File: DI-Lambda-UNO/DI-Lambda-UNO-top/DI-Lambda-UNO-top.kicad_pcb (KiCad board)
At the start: 2 copper layers, 38.2 x 125 mm, 12 parts, among them J1 CONN_02X04, J10 CONN_02X04, J11 CONN_02X04, J12 CONN_02X04, J2 CONN_02X04, J3 CONN_02X04, J4 CONN_02X04, J5 CONN_02X04, J6 CONN_02X04, J7 CONN_02X04, J8 CONN_02X04, J9 CONN_02X04

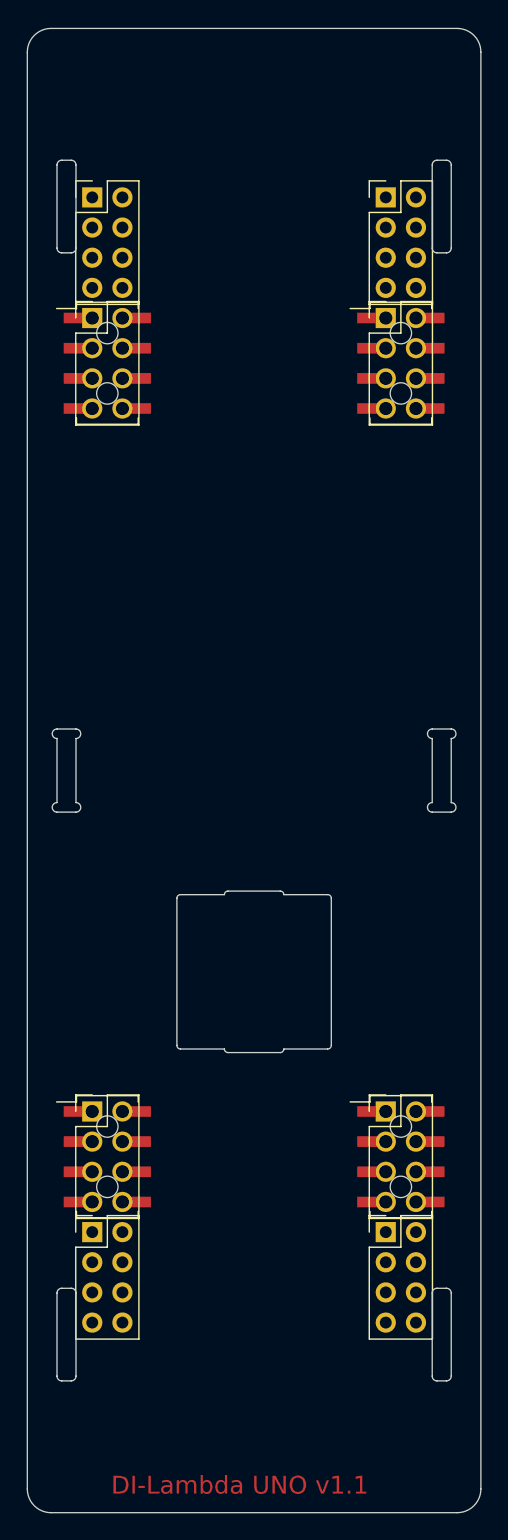
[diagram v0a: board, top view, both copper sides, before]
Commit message: Rework the top plate - STM+THT connectors and new dimensions
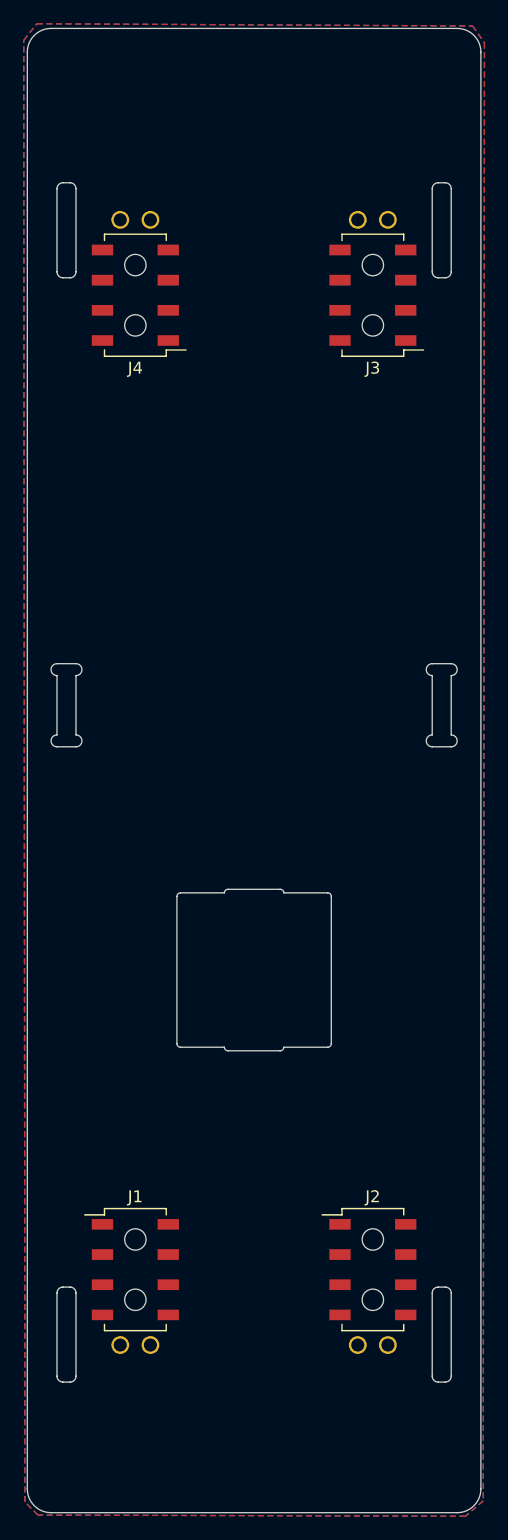
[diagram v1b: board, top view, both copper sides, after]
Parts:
- removed J10, J11, J12, J9: CONN_02X04, Female_socket_pitch254_smt_through-board:Pin_Header_Straight_2x04_Pitch2.54mm_SMD
- removed J5, J6, J7, J8: CONN_02X04, Female_sockets_254_tht:Pin_Header_Straight_2x04_Pitch2.54mm
- J1, J2, J3, J4: footprint Female_sockets_254_tht:Pin_Header_Straight_2x04_Pitch2.54mm -> Female_socket_pitch254_smt_through-board:Pin_Header_Straight_2x04_Pitch2.54mm_SMD_2THT
- moved J1 82.9 mm to (139.2, 123.3)
- moved J3 78.9 mm to (159.2, 41.2), turned to 180 degrees
- moved J2 13.4 mm to (159.2, 123.3)
- moved J4 4.11 mm to (139.2, 41.2), turned to 180 degrees
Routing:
- added copper zone on B.Cu, net (none)
- added copper zone on F.Cu, net (none)
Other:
- outline, holes or cut-outs redrawn

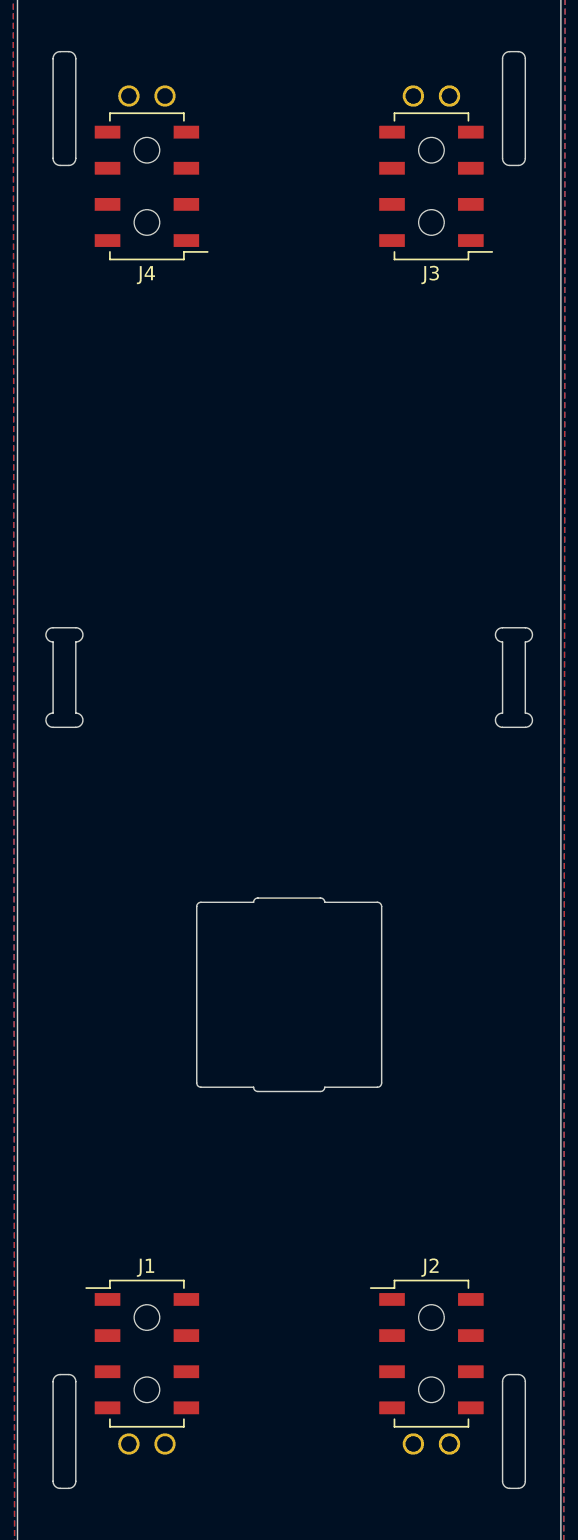
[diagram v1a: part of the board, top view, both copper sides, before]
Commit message: Update schematics to version 1.3
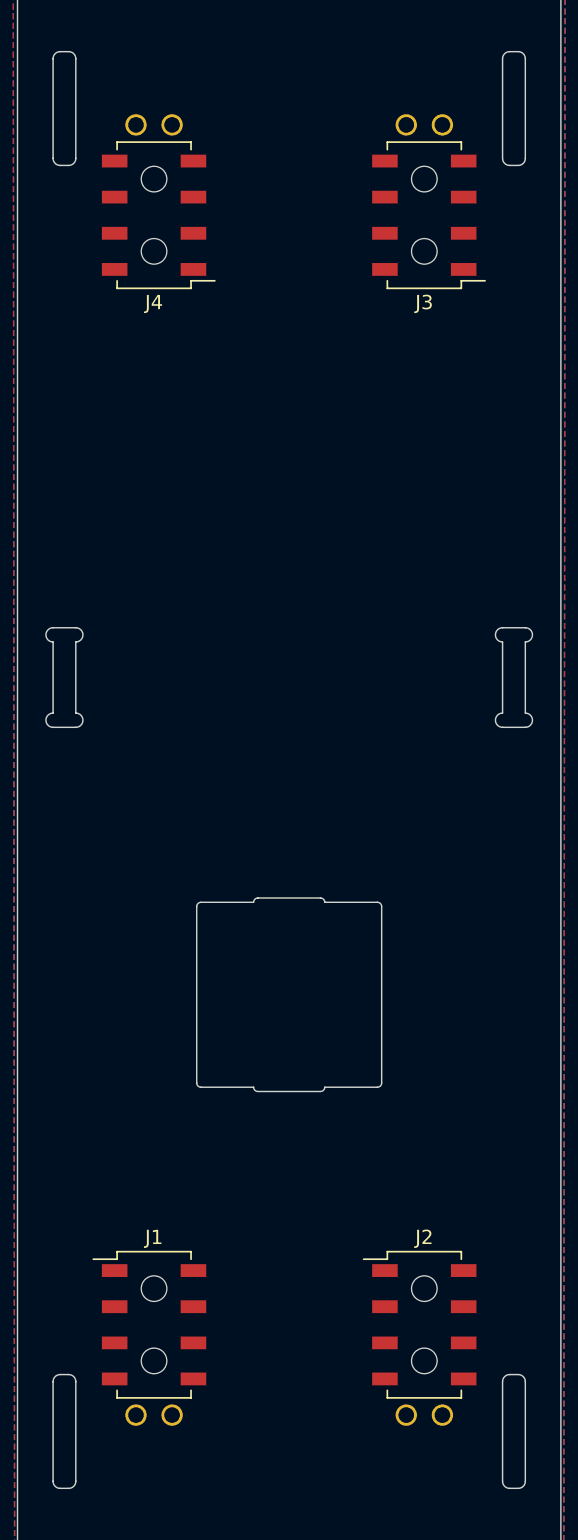
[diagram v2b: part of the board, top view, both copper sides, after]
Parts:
- moved J1 2.09 mm to (139.7, 121.3)
- moved J2 2.09 mm to (158.7, 121.3)
- moved J3 2.09 mm to (158.7, 43.3)
- moved J4 2.09 mm to (139.7, 43.3)
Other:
- board text added: "DI-Lambda UNO v1.3"
- board text removed: "DI-Lambda UNO v1.1"
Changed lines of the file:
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@@
   (general
     (thickness 1.6)
-    (drawings 90)
+    (drawings 98)
     (tracks 0)
     (zones 0)
@@
     (aux_axis_origin 0 0)
     (grid_origin 130.084 143.764)
-    (visible_elements FFFFFF7F)
+    (visible_elements FFFFEF7F)
     (pcbplotparams
       (layerselection 0x000f0_ffffffff)
@@
   )
   (module Female_socket_pitch254_smt_through-board:Pin_Header_Straight_2x04_Pitch2.54mm_SMD_2THT (layer F.Cu)
-    (at 139.184 41.234 180)
+    (at 139.684 43.264 180)
     (descr "surface-mounted straight pin header, 2x04, 2.54mm pitch, double rows")
     (tags "Surface mounted pin header SMD 2x04 2.54mm double row wirth 2 THT holes")
@@
   )
   (module Female_socket_pitch254_smt_through-board:Pin_Header_Straight_2x04_Pitch2.54mm_SMD_2THT (layer F.Cu)
-    (at 159.184 41.234 180)
+    (at 158.684 43.264 180)
     (descr "surface-mounted straight pin header, 2x04, 2.54mm pitch, double rows")
     (tags "Surface mounted pin header SMD 2x04 2.54mm double row wirth 2 THT holes")
@@
   )
   (module Female_socket_pitch254_smt_through-board:Pin_Header_Straight_2x04_Pitch2.54mm_SMD_2THT (layer F.Cu)
-    (at 159.184 123.294)
+    (at 158.684 121.264)
     (descr "surface-mounted straight pin header, 2x04, 2.54mm pitch, double rows")
     (tags "Surface mounted pin header SMD 2x04 2.54mm double row wirth 2 THT holes")
@@
   )
   (module Female_socket_pitch254_smt_through-board:Pin_Header_Straight_2x04_Pitch2.54mm_SMD_2THT (layer F.Cu)
-    (at 139.184 123.294)
+    (at 139.684 121.264)
     (descr "surface-mounted straight pin header, 2x04, 2.54mm pitch, double rows")
     (tags "Surface mounted pin header SMD 2x04 2.54mm double row wirth 2 THT holes")
@@
     (pad "" np_thru_hole circle (at 0 2.54) (size 1.8 1.8) (drill 1.8) (layers *.Cu *.Mask))
   )
+  (gr_text "DI-Lambda UNO v1.3" (at 149.184 23.164) (layer F.Mask)
+    (effects (font (size 1.5 1.5) (thickness 0.3)))
+  )
+  (gr_line (start 139.684 32.264) (end 139.684 136.864) (layer Eco1.User) (width 0.2))
+  (gr_line (start 158.684 121.264) (end 135.484 121.264) (layer Eco1.User) (width 0.2))
+  (gr_line (start 158.684 43.264) (end 135.384 43.264) (layer Eco1.User) (width 0.2))
+  (dimension 78 (width 0.3) (layer Eco1.User)
+    (gr_text "78.000 mm" (at 181.536674 82.264 90) (layer Eco1.User)
+      (effects (font (size 1.5 1.5) (thickness 0.3)))
+    )
+    (feature1 (pts (xy 158.684 43.264) (xy 182.886674 43.264)))
+    (feature2 (pts (xy 158.684 121.264) (xy 182.886674 121.264)))
+    (crossbar (pts (xy 180.186674 121.264) (xy 180.186674 43.264)))
+    (arrow1a (pts (xy 180.186674 43.264) (xy 180.773095 44.390504)))
+    (arrow1b (pts (xy 180.186674 43.264) (xy 179.600253 44.390504)))
+    (arrow2a (pts (xy 180.186674 121.264) (xy 180.773095 120.137496)))
+    (arrow2b (pts (xy 180.186674 121.264) (xy 179.600253 120.137496)))
+  )
+  (dimension 22.5 (width 0.3) (layer Eco1.User)
+    (gr_text "22.500 mm" (at 175.034 132.514 90) (layer Eco1.User)
+      (effects (font (size 1.5 1.5) (thickness 0.3)))
+    )
+    (feature1 (pts (xy 158.684 121.264) (xy 176.384 121.264)))
+    (feature2 (pts (xy 158.684 143.764) (xy 176.384 143.764)))
+    (crossbar (pts (xy 173.684 143.764) (xy 173.684 121.264)))
+    (arrow1a (pts (xy 173.684 121.264) (xy 174.270421 122.390504)))
+    (arrow1b (pts (xy 173.684 121.264) (xy 173.097579 122.390504)))
+    (arrow2a (pts (xy 173.684 143.764) (xy 174.270421 142.637496)))
+    (arrow2b (pts (xy 173.684 143.764) (xy 173.097579 142.637496)))
+  )
+  (dimension 5.5 (width 0.3) (layer Eco1.User)
+    (gr_text "5.500 mm" (at 161.423127 28.360696) (layer Eco1.User)
+      (effects (font (size 1.5 1.5) (thickness 0.3)))
+    )
+    (feature1 (pts (xy 164.173127 32.310696) (xy 164.173127 27.010696)))
+    (feature2 (pts (xy 158.673127 32.310696) (xy 158.673127 27.010696)))
+    (crossbar (pts (xy 158.673127 29.710696) (xy 164.173127 29.710696)))
+    (arrow1a (pts (xy 164.173127 29.710696) (xy 163.046623 30.297117)))
+    (arrow1b (pts (xy 164.173127 29.710696) (xy 163.046623 29.124275)))
+    (arrow2a (pts (xy 158.673127 29.710696) (xy 159.799631 30.297117)))
+    (arrow2b (pts (xy 158.673127 29.710696) (xy 159.799631 29.124275)))
+  )
+  (gr_line (start 158.684 31.964) (end 158.684 136.564) (layer Eco1.User) (width 0.2))
+  (dimension 5.5 (width 0.3) (layer Eco1.User)
+    (gr_text "5.500 mm" (at 136.934 28.314) (layer Eco1.User)
+      (effects (font (size 1.5 1.5) (thickness 0.3)))
+    )
+    (feature1 (pts (xy 139.684 32.264) (xy 139.684 26.964)))
+    (feature2 (pts (xy 134.184 32.264) (xy 134.184 26.964)))
+    (crossbar (pts (xy 134.184 29.664) (xy 139.684 29.664)))
+    (arrow1a (pts (xy 139.684 29.664) (xy 138.557496 30.250421)))
+    (arrow1b (pts (xy 139.684 29.664) (xy 138.557496 29.077579)))
+    (arrow2a (pts (xy 134.184 29.664) (xy 135.310504 30.250421)))
+    (arrow2b (pts (xy 134.184 29.664) (xy 135.310504 29.077579)))
+  )
   (dimension 20.7 (width 0.3) (layer Eco1.User)
-    (gr_text "20.700 mm" (at 138.834 114.914 90) (layer Eco1.User)
-      (effects (font (size 1.5 1.5) (thickness 0.3)))
-    )
-    (feature1 (pts (xy 142.784 104.564) (xy 137.484 104.564)))
-    (feature2 (pts (xy 142.784 125.264) (xy 137.484 125.264)))
-    (crossbar (pts (xy 140.184 125.264) (xy 140.184 104.564)))
-    (arrow1a (pts (xy 140.184 104.564) (xy 140.770421 105.690504)))
-    (arrow1b (pts (xy 140.184 104.564) (xy 139.597579 105.690504)))
-    (arrow2a (pts (xy 140.184 125.264) (xy 140.770421 124.137496)))
-    (arrow2b (pts (xy 140.184 125.264) (xy 139.597579 124.137496)))
+    (gr_text "20.700 mm" (at 150.334 114.914 90) (layer Eco1.User)
+      (effects (font (size 1.5 1.5) (thickness 0.3)))
+    )
+    (feature1 (pts (xy 142.784 104.564) (xy 151.684 104.564)))
+    (feature2 (pts (xy 142.784 125.264) (xy 151.684 125.264)))
+    (crossbar (pts (xy 148.984 125.264) (xy 148.984 104.564)))
+    (arrow1a (pts (xy 148.984 104.564) (xy 149.570421 105.690504)))
+    (arrow1b (pts (xy 148.984 104.564) (xy 148.397579 105.690504)))
+    (arrow2a (pts (xy 148.984 125.264) (xy 149.570421 124.137496)))
+    (arrow2b (pts (xy 148.984 125.264) (xy 148.397579 124.137496)))
   )
   (dimension 13 (width 0.3) (layer Eco1.User)
@@
     (arrow2a (pts (xy 158.884328 91.549383) (xy 158.302244 92.678134)))
     (arrow2b (pts (xy 158.884328 91.549383) (xy 159.475077 92.673623)))
-  )
-  (gr_text "DI-Lambda UNO v1.1" (at 149.284 114.864) (layer F.Mask)
-    (effects (font (size 1.5 1.5) (thickness 0.3)))
   )
   (dimension 15.3 (width 0.3) (layer Eco1.User)
@@
       )
     )
+  )
+  (zone (net 0) (net_name "") (layer F.Cu) (hatch edge 0.508)
+    (connect_pads (clearance 0.508))
+    (min_thickness 0.254)
+    (keepout (tracks not_allowed) (vias not_allowed) (copperpour not_allowed))
+    (fill yes (arc_segments 16) (thermal_gap 0.508) (thermal_bridge_width 0.508))
+    (polygon
+      (pts
+        (xy 161.484 21.964) (xy 161.484 24.264) (xy 136.884 24.264) (xy 136.884 21.964)
+      )
+    )

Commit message: Version 1.5
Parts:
- added C1: 0.1uF 25v, Capacitor_SMD:C_0603_1608Metric, F.Cu at (149.3, 80.7)
- added C10: 0.1uF 25v, Capacitor_SMD:C_0603_1608Metric, F.Cu at (145.2, 87.3)
- added C11: 0.1uF 25v, Capacitor_SMD:C_0603_1608Metric, F.Cu at (161.0, 85.7)
- added C2: 22pF 25V, Capacitor_SMD:C_0603_1608Metric, F.Cu at (145.2, 93.9)
- added C3: 22pF 25V, Capacitor_SMD:C_0603_1608Metric, F.Cu at (145.2, 90.5)
- added C4: 4.7uF 25V, Capacitor_SMD:C_0603_1608Metric, F.Cu at (151.8, 80.7)
- added C5: 1uF 25V, Capacitor_SMD:C_0603_1608Metric, F.Cu at (153.7, 80.7)
- added C8: 0.1uF 25v, Capacitor_SMD:C_0603_1608Metric, F.Cu at (161.0, 92.9)
- added C9: 0.1uF 25v, Capacitor_SMD:C_0603_1608Metric, F.Cu at (149.6, 97.1)
- added J10: Conn_02x02_Odd_Even, Connector_PinSocket_2.54mm:PinSocket_2x02_P2.54mm_Vertical_SMD, F.Cu at (161.9, 66.2)
- added J11: Conn_02x02_Odd_Even, Connector_PinSocket_2.54mm:PinSocket_2x02_P2.54mm_Vertical_SMD, F.Cu at (138.9, 66.2)
- added J12: Conn_01x05, Connector_PinHeader_2.54mm:PinHeader_1x05_P2.54mm_Vertical, B.Cu at (145.3, 62.7)
- added J13: Conn_01x11, Connector_PinHeader_2.54mm:PinHeader_1x11_P2.54mm_Vertical, B.Cu at (137.7, 106.1)
- added J17: CONN_02X03, Connector_PinSocket_2.54mm:PinSocket_2x03_P2.54mm_Vertical_SMD, F.Cu at (140.7, 81.1)
- added J5: Conn_01x11, Connector_PinHeader_2.54mm:PinHeader_1x11_P2.54mm_Vertical, B.Cu at (137.7, 44.7)
- added J6: Conn_02x03_Odd_Even, Board_grooves:Pocket_1.6mm_7mm_no_cap, B.Cu at (166.2, 96.2)
- added J7: Conn_02x03_Odd_Even, Board_grooves:Pocket_1.6mm_7mm_no_cap, B.Cu at (134.6, 96.2)
- added J8: Conn_02x04_Odd_Even, Board_grooves:Pocket_1.6mm_7mm_no_cap, B.Cu at (134.6, 149.2)
- added J9: Conn_02x04_Odd_Even, Board_grooves:Pocket_1.6mm_7mm_no_cap, B.Cu at (166.2, 56.2)
- added MK1: Mounting_Hole, DI-Lambda-module-tabs:Cuvette-cutout-top, F.Cu at (150.4, 118.5)
- added R1: 4.7k, Resistor_SMD:R_0603_1608Metric, F.Cu at (147.2, 80.7)
- added R3: 220R, Resistor_SMD:R_0603_1608Metric, F.Cu at (154.9, 77.0)
- added R4: 220R, Resistor_SMD:R_0603_1608Metric, F.Cu at (146.0, 58.1)
- added R5: 4.7k, Resistor_SMD:R_0603_1608Metric, F.Cu at (140.3, 73.4)
- added R6: 220R, Resistor_SMD:R_0603_1608Metric, F.Cu at (156.9, 58.1)
- added R7: 220R, Resistor_SMD:R_0603_1608Metric, F.Cu at (143.8, 58.1)
- added R9: 4.7k, Resistor_SMD:R_0603_1608Metric, F.Cu at (138.0, 73.4)
- added SW2: SW_BLANK, Button_Switch_SMD:SW_SPST_PTS645, B.Cu at (150.4, 55.0)
- added SW3: SW_SAMPLE, Button_Switch_SMD:SW_SPST_PTS645, B.Cu at (161.4, 55.0)
- added SW4: SW_MODE, Button_Switch_SMD:SW_SPST_PTS645, B.Cu at (139.4, 55.0)
- added U1: LCD_1.44_ST7735, LCD:LCD_1.44_ST7735, B.Cu at (150.4, 74.6)
- added U3: ATMEGA32U4-MU, Housings_QFP:TQFP-44_10x10mm_Pitch0.8mm, F.Cu at (153.2, 89.3)
- added Y1: 8Mhz, Crystals:Crystal_SMD_HC49-SD, F.Cu at (141.0, 93.3)
- J1, J3: value CONN_02X04 -> Conn_02x04_Odd_Even; footprint Female_socket_pitch254_smt_through-board:Pin_Header_Straight_2x04_Pitch2.54mm_SMD_2THT -> Board_grooves:Pocket_1.6mm_7mm_no_cap; moved to B.Cu
- J2, J4: value CONN_02X04 -> Conn_01X01; footprint Female_socket_pitch254_smt_through-board:Pin_Header_Straight_2x04_Pitch2.54mm_SMD_2THT -> Measurement_Points:Measurement_Point_Round-SMD-Pad_Small
- moved J3 106.2 mm to (166.2, 149.2), turned to 270 degrees
- moved J1 65.3 mm to (134.6, 56.2), turned to 270 degrees
- moved J4 57.5 mm to (147.1, 100.3), turned to 0 degrees
- moved J2 25.9 mm to (144.8, 99.4)
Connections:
- J2 pad 1: Net-(J2-Pad1) -> /RX
- J4 pad 1: Net-(J4-Pad1) -> /TX
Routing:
- net /VCC: track 0.00 -> 98.0 mm, vias 0 -> 4
- net /MODE: track 0.00 -> 63.8 mm, vias 0 -> 2
- net /BLANK: track 0.00 -> 52.0 mm, vias 0 -> 2
- net /SAMPLE: track 0.00 -> 45.2 mm, vias 0 -> 2
- net /SDA: track 0.00 -> 43.1 mm, vias 0 -> 2
- net /LED_PWM: track 0.00 -> 42.1 mm
- net GND: track 0.00 -> 41.3 mm, vias 0 -> 12
- net /SCL: track 0.00 -> 36.9 mm, vias 0 -> 2
- net /LCD_A0: track 0.00 -> 35.3 mm, vias 0 -> 1
- net /LCD_LED: track 0.00 -> 32.2 mm, vias 0 -> 2
- net /LCD_RST: track 0.00 -> 32.0 mm, vias 0 -> 1
- net /MOSI: track 0.00 -> 25.7 mm, vias 0 -> 1
- net /DP: track 0.00 -> 24.6 mm
- net /SCK: track 0.00 -> 24.4 mm, vias 0 -> 3
- net /VBUS: track 0.00 -> 23.4 mm, vias 0 -> 2
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- added copper zone on B.Cu, net GND
- added copper zone on F.Cu, net GND
- removed copper zone on B.Cu, net (none)
- removed copper zone on F.Cu, net (none)
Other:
- board size 38.2 x 125 mm -> 38.2 x 128 mm
- board text added: "DI-Lambda UNO v1.5"
- board text added: "RX"
- board text added: "TX"
- board text removed: "DI-Lambda UNO v1.3"
